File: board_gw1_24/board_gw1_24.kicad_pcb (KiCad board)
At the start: 4 copper layers, 29.8 x 15.2 mm, 147 parts, among them J1 USB_C_Receptacle, Q10 2N7002, Q14 2N7002, Q15 2N7002, Q19 2N7002, Q2 2N7002, Q20 2N7002, Q25 2N7002, Q26 2N7002, Q28 2N7002, Q29 2N7002, Q3 2N7002, Q30 2N7002, Q32 2N7002, Q33 2N7002, Q34 2N7002, Q35 2N7002, Q36 2N7002, Q38 2N7002, Q39 2N7002, Q41 2N7002, Q5 2N7002, Q6 2N7002, Q7 2N7002, Q8 2N7002, Q9 2N7002, U1 GW1NR-LV9-QN88-C6/I5, U11 FT232H, U2 ESD224DQA, U3 MIC5203-3.3BM5, U4 APS6404L-3SQR-ZR, U5 MIC5504-1.2YM5, U6 TPS562242, U7 W25Q16JVUXIQ, X1 12MHz

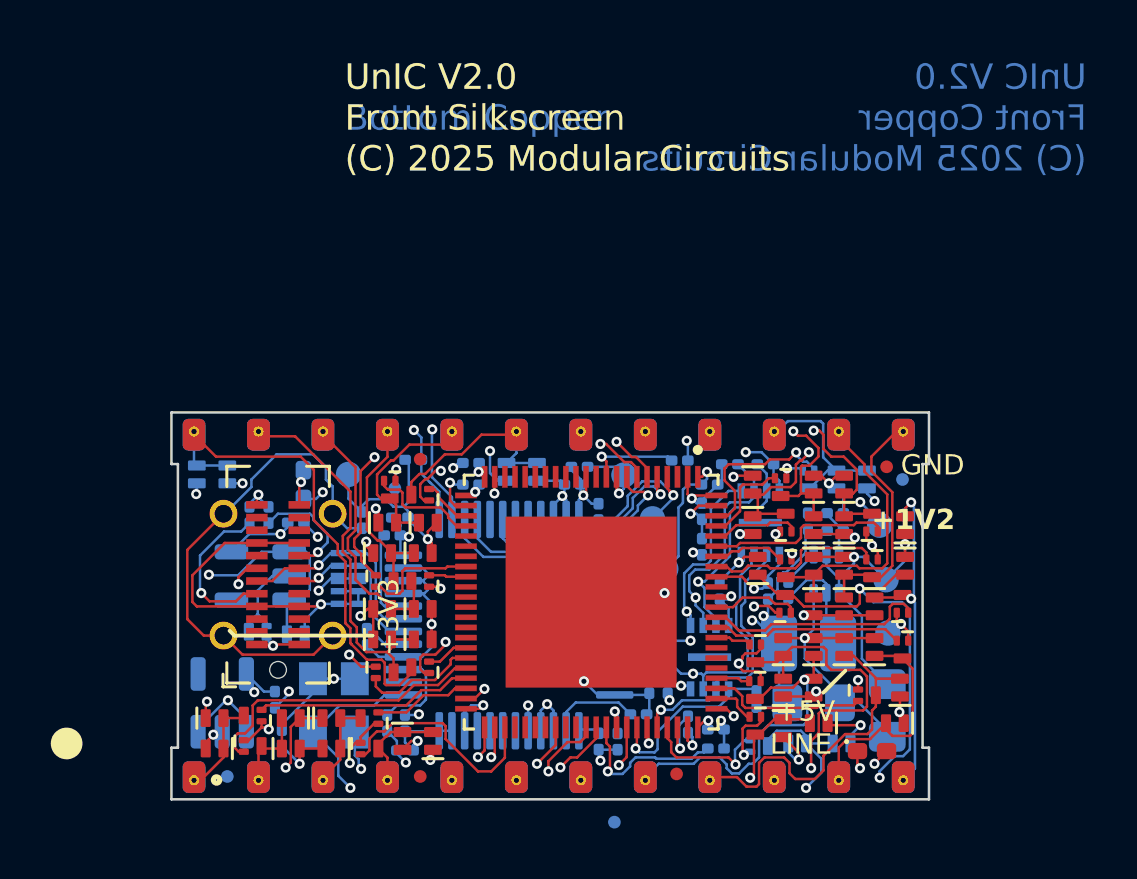
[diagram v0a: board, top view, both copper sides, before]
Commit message: Cleaned up some shapes, added series resistor to clock.
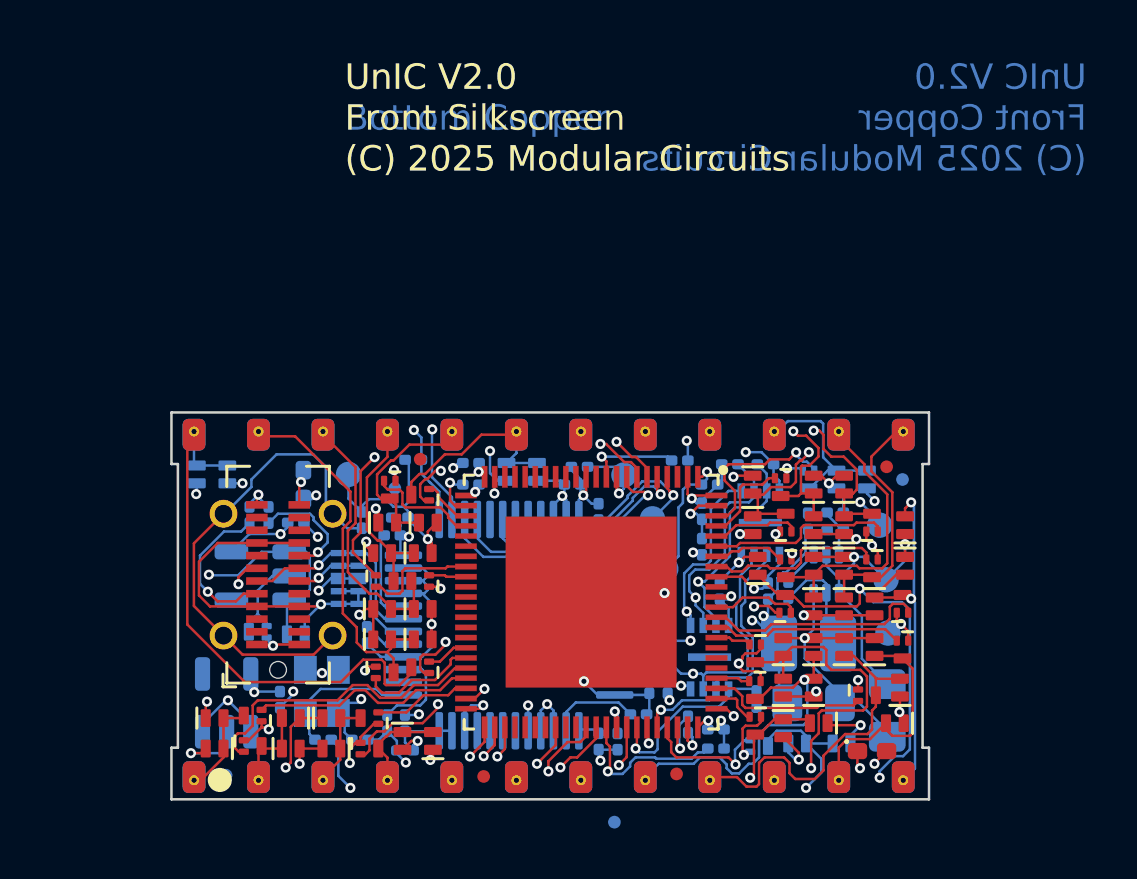
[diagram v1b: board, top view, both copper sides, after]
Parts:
- added R14: 220, Resistor_SMD:R_0201_0603Metric, B.Cu at (54.4, 68.0)
- X1: footprint UNIC:Oscillator_SMD_Abracon_ASE-4Pin_3.2x2.5mm -> UNIC:Oscillator_SMD_2.5x2.0mm
- moved C27 3.08 mm to (55.9, 68.0), turned to 180 degrees
- moved FID3 2.50 mm to (60.7, 69.4)
- moved X1 0.73 mm to (54.4, 66.1)
- moved C2 0.20 mm to (52.7, 66.4)
- moved U5 0.17 mm to (50.6, 66.5)
- moved R21 0.08 mm to (56.1, 63.8)
- moved FID4 0.07 mm to (50.6, 69.4)
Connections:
- U1 pad 52: /CLK1 -> Net-(U1-IOR17A/GCLKT_3)
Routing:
- net Net-(U1-IOR17A/GCLKT_3): track 0.00 -> 11.7 mm, vias 0 -> 2
- net /CLK1: track 16.5 -> 5.64 mm, vias 2 -> 0
- net /PIN24: track 19.2 -> 21.5 mm
- net GND: track 85.0 -> 86.7 mm
- net +3V3: track 117.7 -> 116.3 mm
- net Net-(J1-SHIELD): track 20.1 -> 19.4 mm
- net LINE: track 109.5 -> 110.1 mm
- net /PIN4_F: track 8.97 -> 8.69 mm, vias 0 -> 2
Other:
- board text added: "UnIC V2"
- board text removed: "(C) 2025"
- board text removed: "+1V2"
- board text removed: "+3V3"
- board text removed: "+5V"
- board text removed: "GND"
- board text removed: "LINE"
- board text removed: "Modular Circuits"
- board text removed: "UnIC"
- board text removed: "V2.0"
- board text removed: "~{JTAG_SEL}"
- board text removed: "~{RECONFIG}"

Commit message: Planes are flooded for 24-pin design.
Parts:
- moved C27 0.45 mm to (55.9, 68.4)
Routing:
- net LINE: track 110.1 -> 43.1 mm
- net +3V3: track 116.3 -> 54.0 mm
- net +5V: track 122.6 -> 61.8 mm, vias 18 -> 17
- net +1V2: track 57.9 -> 22.9 mm
- net /PIN15_F: track 6.78 -> 7.99 mm
- net GND: track 86.7 -> 87.6 mm, vias 34 -> 33
- net Net-(U1-IOR17A/GCLKT_3): track 11.7 -> 12.3 mm
- net Net-(LED_DONE1-A): track 27.7 -> 27.1 mm
- added copper zone on In1.Cu, net +1V2
- added copper zone on In2.Cu, net +1V2
- added copper zone on In1.Cu, net +3V3
- added copper zone on In1.Cu, net +5V
- added copper zone on In2.Cu, net +5V
- added copper zone on In1.Cu, net LINE
- added copper zone on In2.Cu, net LINE
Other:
- board text added: "UnIC-24 V2.0 Bottom Fab Drawing (C) 2025 Modular Circuits"
- board text added: "UnIC-24 V2.0 Bottom Mask (C) 2025 Modular Circuits"
- board text added: "UnIC-24 V2.0 Bottom Paste (C) 2025 Modular Circuits"
- board text added: "UnIC-24 V2.0 Bottom Silkscreen (C) 2025 Modular Circuits"
- board text added: "UnIC-24 V2.0 Front Copper (C) 2025 Modular Circuits"
- board text added: "UnIC-24 V2.0 Front Fab Drawing (C) 2025 Modular Circuits"
- board text added: "UnIC-24 V2.0 Front Mask (C) 2025 Modular Circuits"
- board text added: "UnIC-24 V2.0 Front Paste (C) 2025 Modular Circuits"
- board text added: "UnIC-24 V2.0 Front Silkscreen (C) 2025 Modular Circuits"
- board text added: "UnIC-24 V2.0 Layer 2 Copper (C) 2025 Modular Circuits"
- board text added: "UnIC-24 V2.0 Layer 3 Copper (C) 2025 Modular Circuits"
- board text added: "UnIC-24 V2.0 Top Copper (C) 2025 Modular Circuits"
- board text removed: "UnIC V2.0 Bottom Copper (C) 2025 Modular Circuits"
- board text removed: "UnIC V2.0 Bottom Fab Drawing (C) 2025 Modular Circuits"
- board text removed: "UnIC V2.0 Bottom Mask (C) 2025 Modular Circuits"
- board text removed: "UnIC V2.0 Bottom Paste (C) 2025 Modular Circuits"
- board text removed: "UnIC V2.0 Bottom Silkscreen (C) 2025 Modular Circuits"
- board text removed: "UnIC V2.0 Front Copper (C) 2025 Modular Circuits"
- board text removed: "UnIC V2.0 Front Fab Drawing (C) 2025 Modular Circuits"
- board text removed: "UnIC V2.0 Front Mask (C) 2025 Modular Circuits"
- board text removed: "UnIC V2.0 Front Paste (C) 2025 Modular Circuits"
- board text removed: "UnIC V2.0 Front Silkscreen (C) 2025 Modular Circuits"
- board text removed: "UnIC V2.0 Layer 2 Copper (C) 2025 Modular Circuits"
- board text removed: "UnIC V2.0 Layer 3 Copper (C) 2025 Modular Circuits"
